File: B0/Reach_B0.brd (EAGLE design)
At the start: 107.3 x 69.5 mm, 240 parts, among them IC1 TMC2100-LA, IC10 74AHC1G126DCK, IC11 74AHC1G126DCK, IC18 74AHC1G126DCK, IC2 TMC2100-LA, IC3 74AHC1G126DCK, IC4 74AHC1G126DCK, IC5 74AHC1G126DCK, IC6 74AHC1G126DCK, IC7 74AHC1G126DCK, IC8 TMC2100-LA, IC9 74AHC1G126DCK, P8 F-2X23-, P9 F-2X23-, Q2 AON6758, Q3 AON6758, U1 SN74AHC595PW, U10 RT8268, U11 PCA9685PW, U18 CAT24C256, U2 SN74AHC595PW, U3 MCP9600, U4 MCP9600, U5 MCP9600, U6 MCP9600, U7 SN74AHC595PW, X1 22-05-7028-02, X11 22-05-7028-02, X14 22-05-7048-04, X2 MSTBA4, X21 MSTBA2, X3 MSTBA2, X4 22-05-7028-02, X5 22-05-7028-02, X6 22-05-7048-04, X7 22-05-7028-02, X8 22-05-7048-04, X9 22-05-7028-02

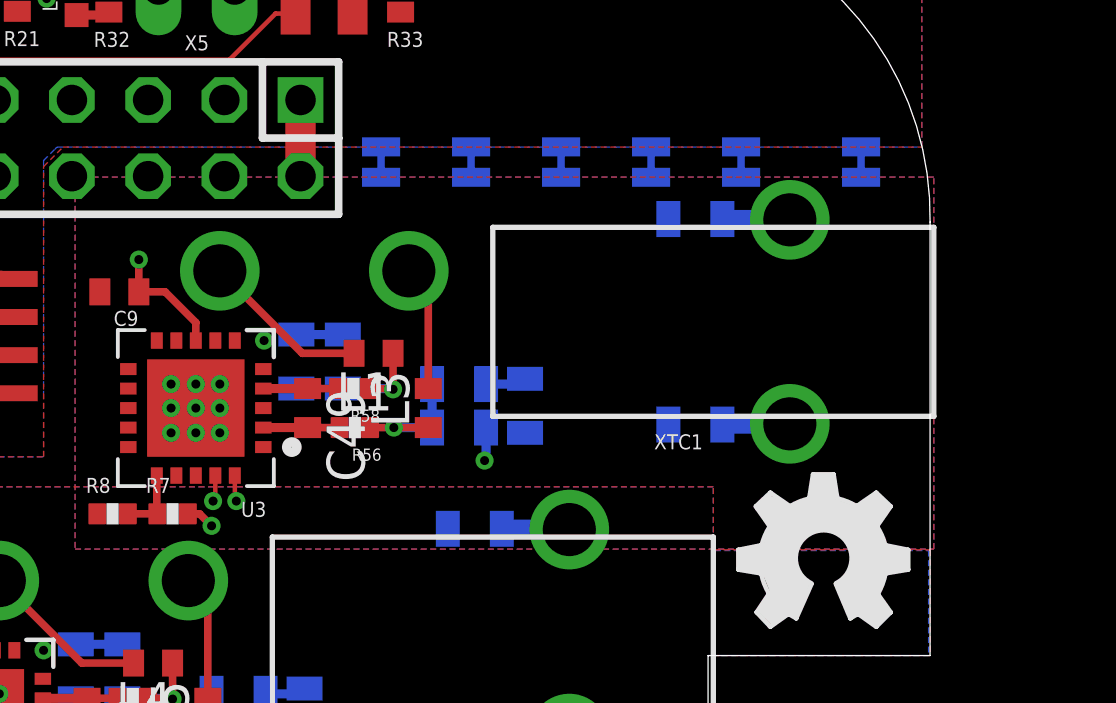
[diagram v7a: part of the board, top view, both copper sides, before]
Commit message: TMC2130
Updated to TMC2130 for stepper driver, testing screw terminal layout for thermocouple connections (thermocouple connectors too expensive).
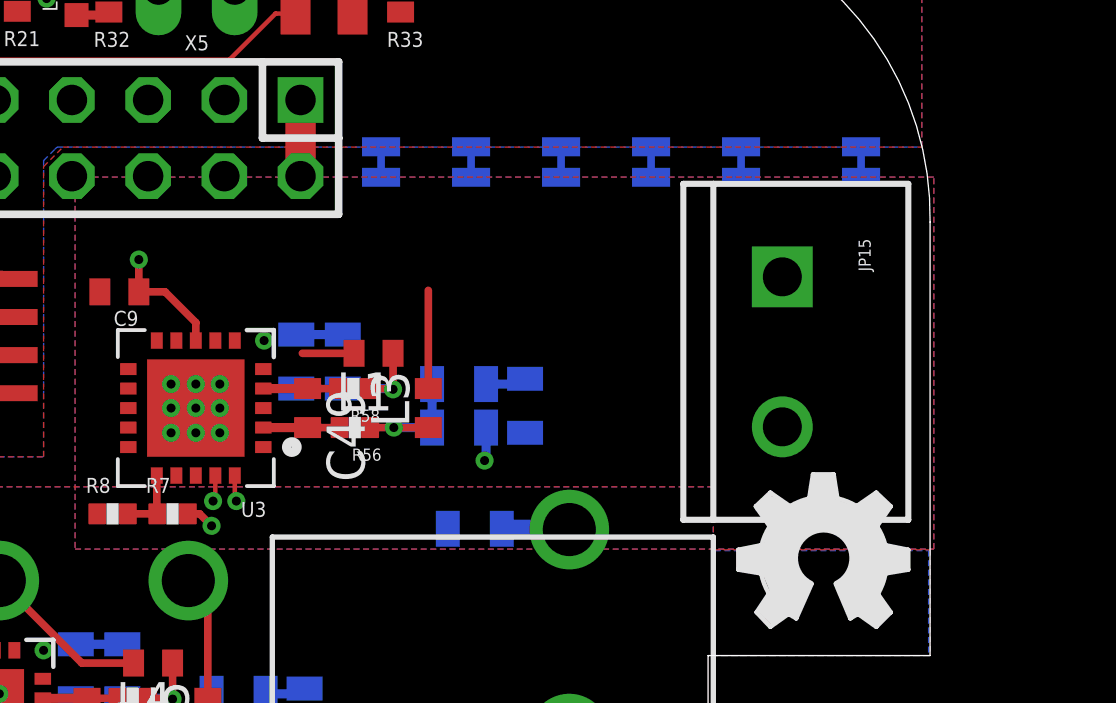
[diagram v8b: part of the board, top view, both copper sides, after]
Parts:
- removed R61, R62: 0, SparkFun-Resistors:0805
- removed XTC1: NEWPORT_THERMOCOUPLE_CONNECTORPCC-SMP-V, reach_custom:PCC-SMP-V
- added JP15: (no value), SparkFun-Connectors:SCREWTERMINAL-5MM-2
- IC1, IC2, IC8: value TMC2100-LA -> TMC2130QFN36; device we-chip:QFN36-PAD -> reach_custom:QFN36
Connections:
- removed net N$51: R61.2, XTC1.P$1
- removed net N$73: R62.2, XTC1.P$2
- net GND: no longer IC1.11, IC2.11, IC8.11
- net GNDI: no longer R61.1, R62.1
- net N$14: now also JP15.1; no longer XTC1.P$3
- net N$15: now also JP15.2; no longer XTC1.P$4
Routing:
- net N$15: track 5.61 -> 1.72 mm
- net N$73: track 2.26 -> 0.00 mm
- net N$51: track 2.26 -> 0.00 mm
- net N$14: track 4.19 -> 3.27 mm
